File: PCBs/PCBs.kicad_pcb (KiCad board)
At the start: 4 copper layers, 29.8 x 11.3 mm, 8 parts, among them U6 TPS62172DSG

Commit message: should be done
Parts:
- removed BuckConverter3-17V->3.3V-C1: 10uF, Capacitor_Tantalum_SMD:CP_EIA-1608-10_AVX-L
- removed BuckConverter3-17V->3.3V-C2: 22uF, Capacitor_Tantalum_SMD:CP_EIA-1608-10_AVX-L
- removed BuckConverter3-17V->3.3V-L1: 2.2 uH, Inductor_SMD:L_1008_2520Metric_Pad1.43x2.20mm_HandSolder
- removed BuckConverter3-17V->3.3V-LED1: LED, LED_SMD:LED_0201_0603Metric_Pad0.64x0.40mm_HandSolder
- removed BuckConverter3-17V->3.3V-R1: 100k Ohms, Resistor_SMD:R_0402_1005Metric_Pad0.72x0.64mm_HandSolder
- removed BuckConverter3-17V->3.3V-ScrewTerminalInput1: Input, TerminalBlock_4Ucon:TerminalBlock_4Ucon_1x02_P3.50mm_Horizontal
- removed BuckConverter3-17V->3.3V-ScrewTerminalOutput1: Output, TerminalBlock_4Ucon:TerminalBlock_4Ucon_1x02_P3.50mm_Horizontal
- removed U6: TPS62172DSG, Package_SON:WSON-8-1EP_2x2mm_P0.5mm_EP0.9x1.6mm_ThermalVias
- added C1: 10 uF, EasyEDA2KicadFootprints:C0603, F.Cu at (143.3, 114.9)
- added C2: 22 uF, EasyEDA2KicadFootprints:C0805, F.Cu at (158.2, 117.6)
- added L1: 2.2uH, EasyEDA2KicadFootprints:IND-SMD_L4.0-W4.0_LQH44PN2R2MP0L, F.Cu at (152.0, 114.7)
- added LED1: Green LED, EasyEDA2KicadFootprints:LED-SMD_L0.7-W0.4-RD_GREEN, F.Cu at (147.4, 112.3)
- added P1: Input 1x2, EasyEDA2KicadFootprints:CONN-TH_2P-P5.00_WJ128V-5.0-2P, F.Cu at (136.4, 114.6)
- added P2: Output 1x2, EasyEDA2KicadFootprints:CONN-TH_2P-P5.00_WJ128V-5.0-2P, F.Cu at (166.0, 114.7)
- added R1: 100k Ohms, EasyEDA2KicadFootprints:R0402, F.Cu at (149.1, 110.8)
- added U1: TPS62172DSGR, EasyEDA2KicadFootprints:WSON-8_L2.0-W2.0-P0.50-TL-EP, F.Cu at (146.4, 115.0)
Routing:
- net VCCOUT: track 24.0 -> 43.2 mm, vias 1 -> 4
- net Net-(U1-SW): track 0.00 -> 2.80 mm
- net Net-(U6-SW): track 2.65 -> 0.00 mm
- net Net-(BuckConverter3-17V->3.3V-LED1-K): track 1.96 -> 0.00 mm
- net Net-(LED1-A): track 0.00 -> 1.84 mm
- net Net-(LED1-K): track 0.00 -> 1.60 mm
- net Net-(BuckConverter3-17V->3.3V-LED1-A): track 1.20 -> 0.00 mm
- net VCCIN: track 3.95 -> 3.31 mm
- removed copper zone on In1.Cu, net GND
- removed copper zone on In2.Cu, net VCCIN
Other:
- board size 29.8 x 11.3 mm -> 44.5 x 15.5 mm
- board text removed: "C1"
- board text removed: "C2"
- board text removed: "Input"
- board text removed: "L1"
- board text removed: "Output"
- board text removed: "R1"
- board text removed: "TPS62172DSGR"

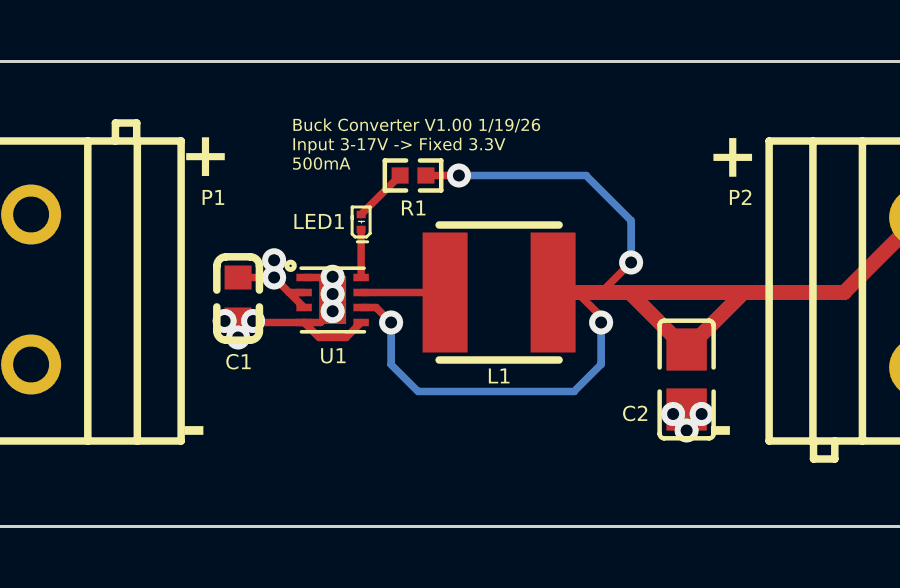
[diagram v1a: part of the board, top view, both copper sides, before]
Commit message: buck converter done
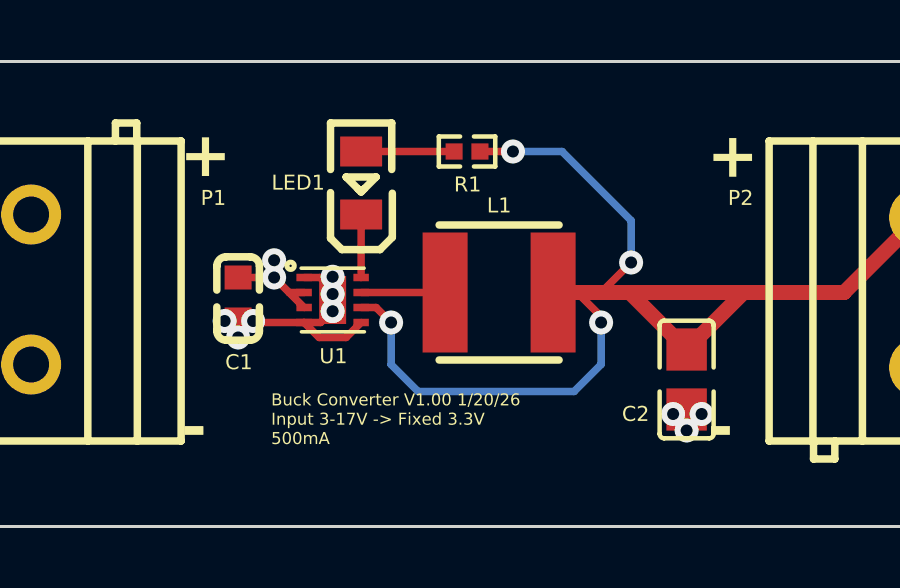
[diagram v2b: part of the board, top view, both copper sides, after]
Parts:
- LED1: footprint EasyEDA2KicadFootprints:LED-SMD_L0.7-W0.4-RD_GREEN -> EasyEDA2KicadFootprints:LED0805-R-RD
- moved R1 1.97 mm to (150.9, 110.0)
- moved LED1 1.30 mm to (147.4, 111.0)
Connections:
- LED1 pad 1: Net-(LED1-K) -> Net-(LED1-A)
- LED1 pad 2: Net-(LED1-A) -> Net-(LED1-K)
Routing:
- net VCCOUT: track 43.2 -> 41.8 mm
- net Net-(LED1-A): track 1.84 -> 3.10 mm
- net Net-(LED1-K): track 1.60 -> 2.10 mm
- added copper zone on In1.Cu, net GND
- added copper zone on In2.Cu, net VCCIN
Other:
- board text added: "Buck Converter V1.00 1/20/26 Input 3-17V -> Fixed 3.3V 500mA"
- board text removed: "Buck Converter V1.00 1/19/26 Input 3-17V -> Fixed 3.3V 500mA"
